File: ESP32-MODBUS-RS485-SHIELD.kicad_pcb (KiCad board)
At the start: 2 copper layers, 55 x 29.4 mm, 27 parts, among them J1 Conn_01x19, J10 Conn_01x02, J2 Conn_01x19, J9 RS485, Q17 WST3400S, Q18 WST3400S, Q19 WST3400S, U11 SN75176AD

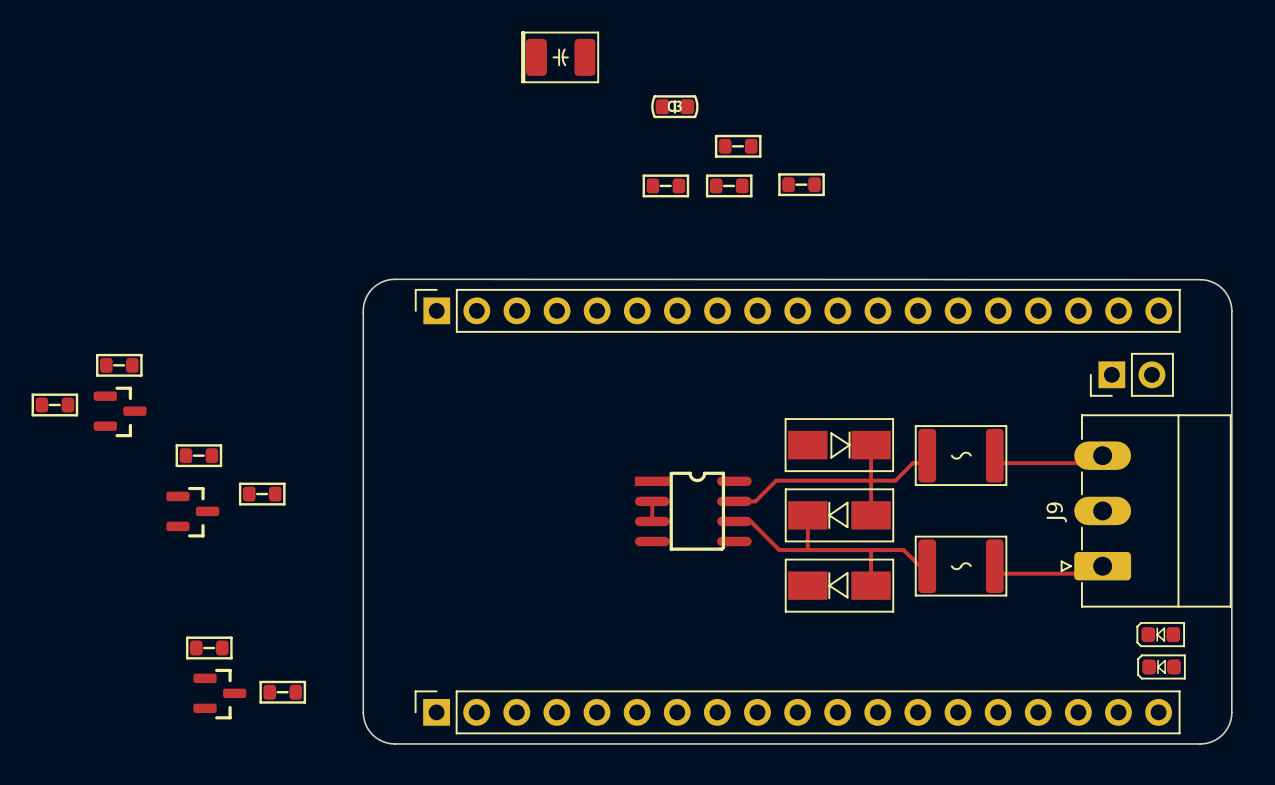
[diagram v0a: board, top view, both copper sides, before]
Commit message: Update ESP32-MODBUS-RS485-SHIELD.kicad_pcb
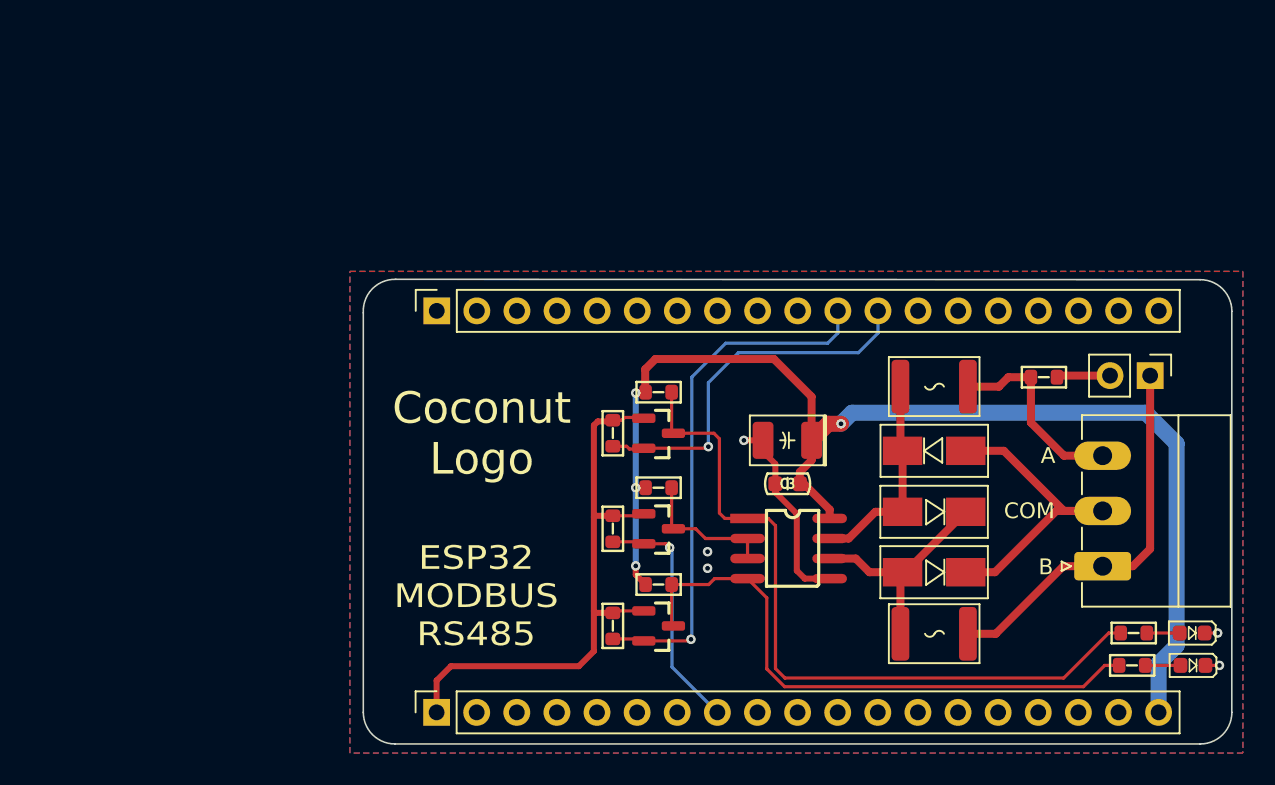
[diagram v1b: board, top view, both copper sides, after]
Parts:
- removed R1: 4.7k, Library:R_0603_1608Metric
- R36: value 4.7k -> 120
- moved R47 39.7 mm to (165.6, 101.9)
- moved R45 36.9 mm to (165.5, 104.0)
- moved R41 35.4 mm to (132.7, 89.2), turned to -90 degrees
- moved R40 34.2 mm to (135.6, 86.7)
- moved Q18 34.1 mm to (135.6, 89.2)
- moved Q19 29.5 mm to (135.6, 95.3)
- moved R38 28.7 mm to (135.6, 98.8)
- moved C5 28.2 mm to (143.7, 89.7), turned to 180 degrees
- moved Q17 28.1 mm to (135.6, 101.5)
- moved R36 26.8 mm to (159.9, 85.7)
- moved R43 26.6 mm to (132.7, 95.3), turned to -90 degrees
- moved R42 25.1 mm to (135.6, 92.7)
- moved C3 24.9 mm to (143.7, 92.5), turned to 180 degrees
- moved R39 21.3 mm to (132.7, 101.5), turned to -90 degrees
- moved U11 6.47 mm to (143.8, 96.5)
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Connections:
- D33 pad 1: /B -> Net-(D33-A1)
- D33 pad 2: /A -> Net-(D33-A2)
- D34 pad 2: /B -> Net-(D33-A1)
- D35 pad 1: /A -> Net-(D33-A2)
- F1 pad 1: /A -> Net-(D33-A2)
- F1 pad 2: Net-(J9-Pin_3) -> /A
- F2 pad 1: /B -> Net-(D33-A1)
- F2 pad 2: Net-(J10-Pin_1) -> /B
- J1 pad 8: /GPIO33 -> /RS485_DE
- J10 pad 1: Net-(J10-Pin_1) -> /B
- J2 pad 11: /GPIO17 -> /RS485_TX
- J2 pad 12: /GPIO16 -> /RS485_RX
- J9 pad 1: Net-(J10-Pin_1) -> /B
- J9 pad 3: Net-(J9-Pin_3) -> /A
- Q17 pad 2: /D_3V3 -> /RS485_TX
- Q18 pad 2: /R_3V3 -> /RS485_RX
- Q19 pad 2: /DE_3V3 -> /RS485_DE
- R36 pad 1: Net-(J9-Pin_3) -> /A
- R39 pad 2: /D_3V3 -> /RS485_TX
- R41 pad 2: /R_3V3 -> /RS485_RX
- R43 pad 2: /DE_3V3 -> /RS485_DE
- U11 pad 6: /B -> Net-(D33-A1)
- U11 pad 7: /A -> Net-(D33-A2)
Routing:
- net /5V: track 0.00 -> 78.0 mm, vias 0 -> 4
- net /R_5V: track 0.00 -> 46.6 mm
- net /D_5V: track 0.00 -> 37.2 mm
- net /3V3: track 0.00 -> 36.9 mm
- net /RS485_TX: track 0.00 -> 33.5 mm, vias 0 -> 1
- net /RS485_RX: track 0.00 -> 23.7 mm, vias 0 -> 1
- net /RS485_COM: track 0.00 -> 20.5 mm
- net /RS485_DE: track 0.00 -> 15.4 mm, vias 0 -> 1
- net Net-(D33-A1): track 0.00 -> 14.5 mm
- net GND: track 0.00 -> 14.3 mm, vias 0 -> 5
- net Net-(D33-A2): track 0.00 -> 13.3 mm
- net /DE_5V: track 1.27 -> 8.86 mm
- net Net-(J9-Pin_3): track 6.83 -> 0.00 mm
- net Net-(J10-Pin_1): track 6.83 -> 0.00 mm
- net /B: track 18.1 -> 24.7 mm
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- added copper zone on B.Cu, net GND
- added copper zone on F.Cu, net GND
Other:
- board text added: "A"
- board text added: "B"
- board text added: "COM"
- board text added: "Coconut Logo"
- board text added: "ESP32 MODBUS RS485"

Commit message: update
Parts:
- added F3: Polyfuse_Small, Fuse:Fuse_1206_3216Metric, F.Cu at (143.6, 86.7)
- moved D36 2.59 mm to (166.8, 104.0)
- moved D37 2.54 mm to (166.8, 101.9)
- moved R47 2.54 mm to (163.1, 101.9)
- moved R45 2.44 mm to (163.1, 104.0)
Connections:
- J1 pad 19: /5V -> Net-(J1-Pin_19)
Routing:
- net /5V: track 78.0 -> 34.0 mm, vias 4 -> 3
- net Net-(J1-Pin_19): track 0.00 -> 42.1 mm, vias 0 -> 2
- net /R_5V: track 46.6 -> 42.0 mm
- net /D_5V: track 37.2 -> 32.7 mm
- net GND: track 14.3 -> 14.7 mm, vias 5 -> 33
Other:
- board text added: "DE"
- board text added: "RX"
- board text added: "TX"

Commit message: Update ESP32-MODBUS-RS485-SHIELD.kicad_pcb
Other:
- board text added: "COCOtronex"
- board text removed: "Coconut Logo"
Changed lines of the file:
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@@
       (plot_on_all_layers_selection 0x0000000_00000000)
       (disableapertmacros false)
-      (usegerberextensions false)
-      (usegerberattributes true)
-      (usegerberadvancedattributes true)
-      (creategerberjobfile true)
+      (usegerberextensions true)
+      (usegerberattributes false)
+      (usegerberadvancedattributes false)
+      (creategerberjobfile false)
       (dashed_line_dash_ratio 12.000000)
       (dashed_line_gap_ratio 3.000000)
@@
       (psa4output false)
       (plotreference true)
-      (plotvalue true)
+      (plotvalue false)
       (plotinvisibletext false)
       (sketchpadsonfab false)
-      (subtractmaskfromsilk false)
+      (subtractmaskfromsilk true)
       (outputformat 1)
       (mirror false)
-      (drillshape 1)
+      (drillshape 0)
       (scaleselection 1)
-      (outputdirectory "")
+      (outputdirectory "Gerber/")
     )
   )
@@
     (fp_line (start 9.45 8) (end 9.45 -1.2)
       (stroke (width 0.1) (type solid)) (layer "F.Fab"))
-    (pad "1" thru_hole roundrect (at 0 0 90) (size 1.8 3.6) (drill 1.2) (layers *.Cu *.Mask) (roundrect_rratio 0.138889)
+    (pad "1" thru_hole roundrect (at 0 0 90) (size 1.8 3.6) (drill 1.2) (layers *.Cu *.Mask) (roundrect_rratio 0.1388888889)
       (net 39 "/B") (pinfunction "Pin_1") (pintype "passive"))
     (pad "2" thru_hole oval (at 3.5 0 90) (size 1.8 3.6) (drill 1.2) (layers *.Cu *.Mask)
@@
     (effects (font (size 1.5 1.7) (thickness 0.3)) (justify bottom))
   )
-  (gr_text "Coconut\nLogo" (at 124.35 92.05) (layer "F.SilkS")
+  (gr_text "COCOtronex" (at 128.3 85.8) (layer "F.SilkS")
     (effects (font (size 2 2) (thickness 0.3)) (justify bottom))
   )

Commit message: update
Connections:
- F1 pad 2: /A -> /B
- F2 pad 2: /B -> /A
- J10 pad 1: /B -> /A
- J9 pad 1: /B -> /A
- J9 pad 3: /A -> /B
- R36 pad 1: /A -> /B
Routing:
- net /B: track 24.7 -> 12.5 mm
- net /A: track 12.5 -> 24.7 mm
